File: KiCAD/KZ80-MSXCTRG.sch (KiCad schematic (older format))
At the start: 14 parts, among them J1 MSX SLOT-A, J2 SBC8080 BUS, J3 MEM-SLOT, J4 Z80 CTRL, J5 PPI PORT-A, U1 74HC139, U2 74HC153, U3 74HC32, U4 74HC00

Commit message: 割り込み信号を外部端子と切り替えるジャンパ装備
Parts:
- removed J3: MEM-SLOT, symbol Connector_Generic:Conn_01x02
- added C5, C6: 10u, symbol Device:CP
- added J3: SLT-JP, symbol Connector_Generic:Conn_01x05
- added JP1: INT_JP, symbol Jumper:Jumper_3_Open
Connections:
- net GND: now also C5.1, C6.1; no longer U4.12, U4.13
- net VCC: now also C5.2, C6.2
- net ~CS1: now also U4.1; no longer U4.4
- net ~CS12: now also U4.6; no longer U4.8
- net ~CS2: now also U4.2; no longer U4.5
- net ~INT: now also JP1.1 (A); no longer J1.8 (Pin_8)
- net ~RFSH: now also U4.10, U4.9; no longer U4.1, U4.2
- net ~SLT0: now also J3.1 (Pin_1)
- net ~SLT2: now also J3.2 (Pin_2)
- net ~SLT3: now also U4.12, U4.13, J3.3 (Pin_3)
- net at U3.2: now also U4.8; no longer U4.3
- net at U4.11: now also J3.4 (Pin_4)
- new net: U4.3, U4.4, U4.5
- new net ~INT-J: J3.5 (Pin_5), JP1.3 (B)
- new net ~INT-S: J1.8 (Pin_8), JP1.2 (C)
- no-connect marks 36 -> 34
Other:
- note added: "FRONT SIDE"
- moved on the sheet: C2, C3, C4, U1C, U3B, U3C, U3D, U3E, U4D, U4E

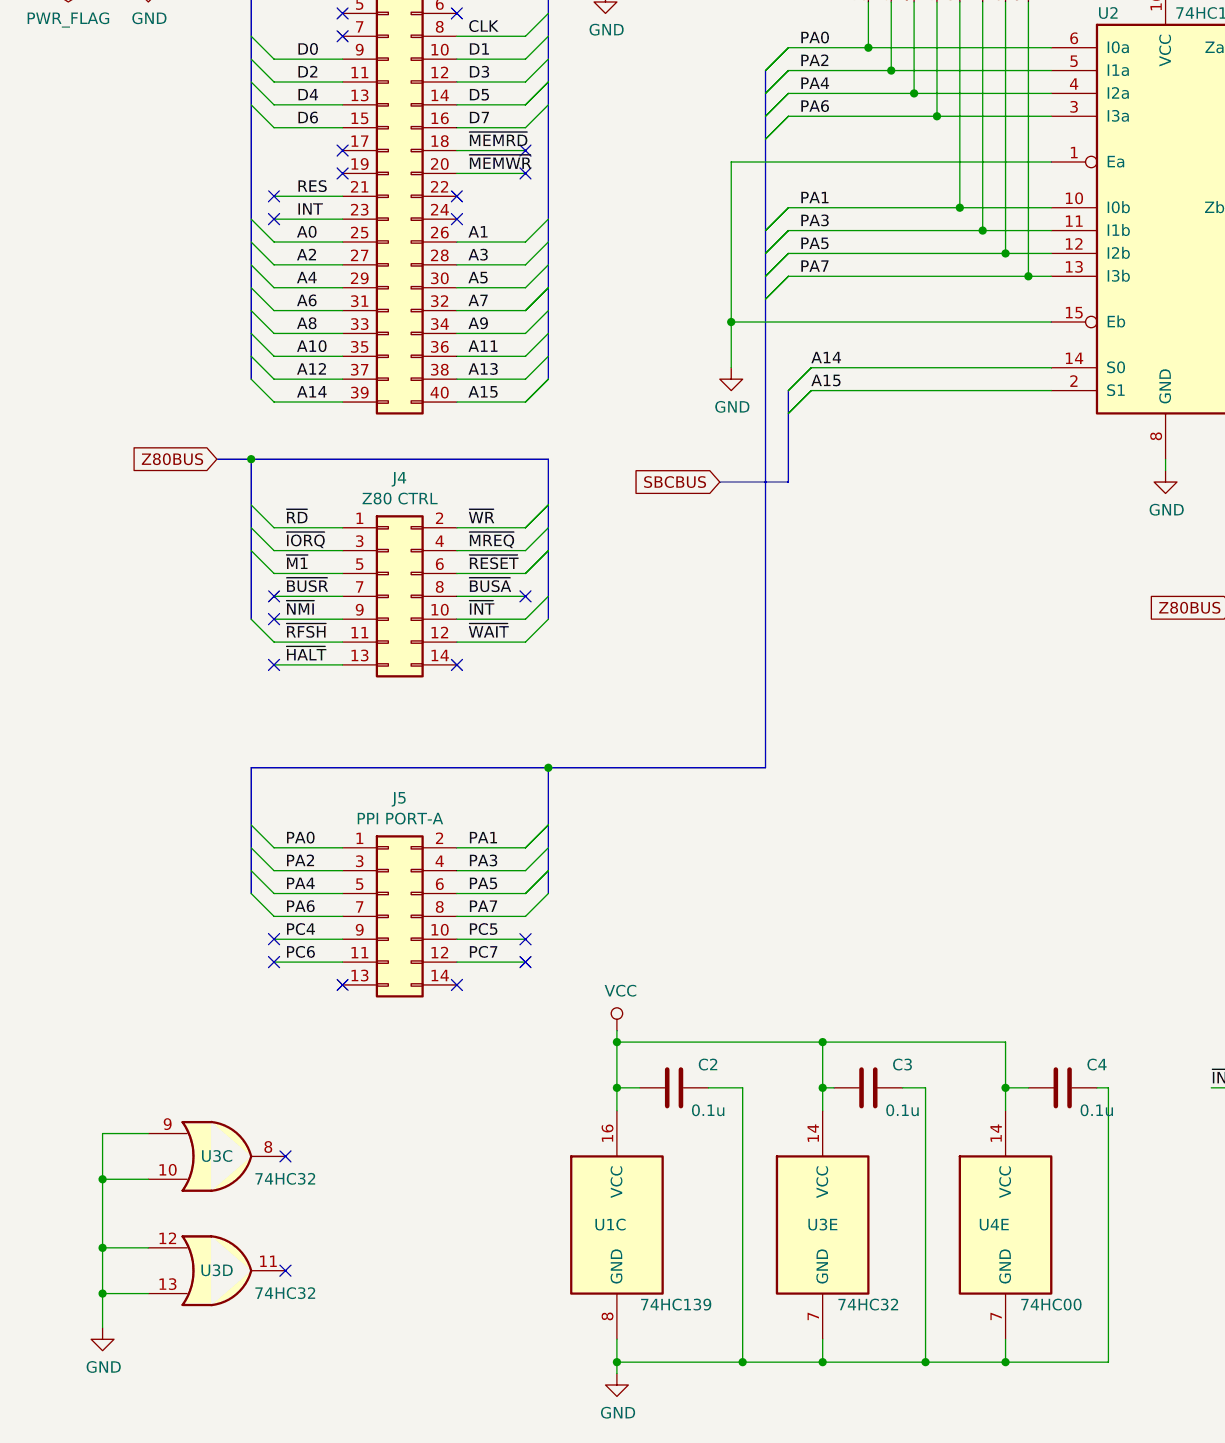
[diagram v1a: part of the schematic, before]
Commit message: 74HC153コントロールをPPI出力で暫定実施
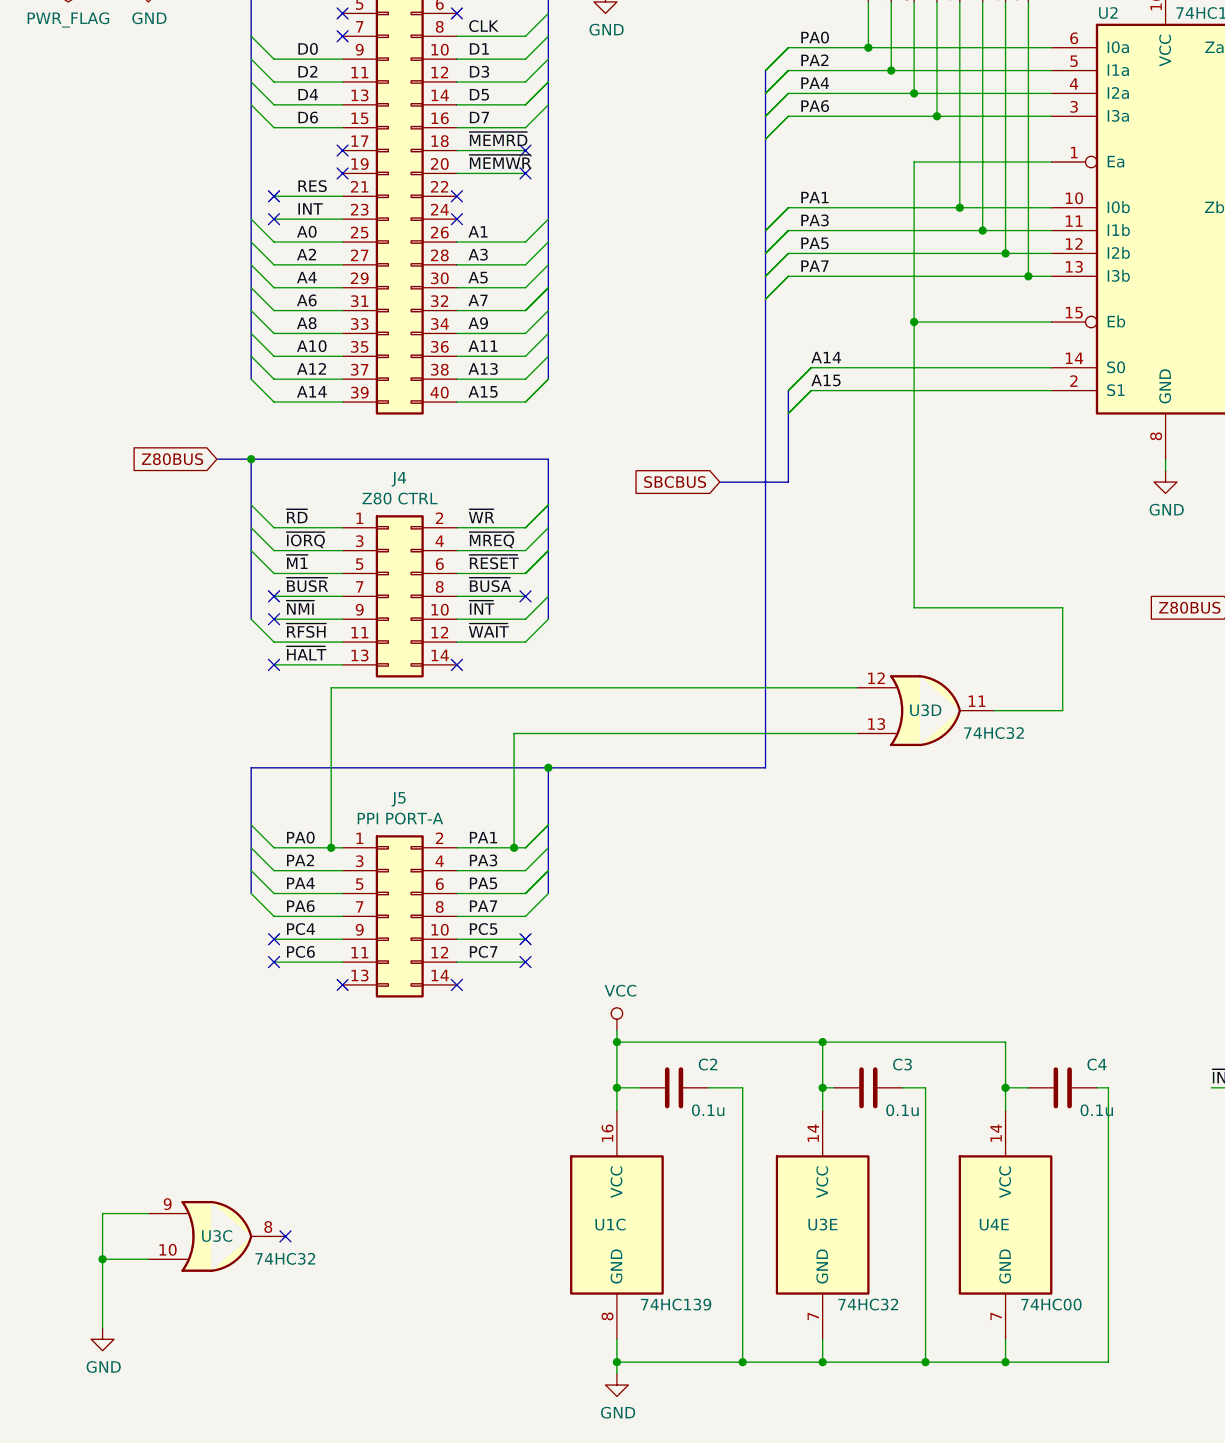
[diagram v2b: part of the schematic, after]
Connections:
- net GND: no longer U2.1 (Ea), U2.15 (Eb), U3.12, U3.13
- net PA0: now also U3.12
- net PA1: now also U3.13
- net at U3.11: now also U2.1 (Ea), U2.15 (Eb)
- no-connect marks 34 -> 33
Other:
- moved on the sheet: U3C, U3D
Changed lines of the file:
@@
 $EndComp
 Wire Wire Line
-	1600 5250 1900 5250
+	1600 5250 1850 5250
 Wire Wire Line
 	1600 5350 1900 5350
@@
 	1500 5450 1600 5550
 Wire Wire Line
-	2400 5250 2700 5250
+	2400 5250 2650 5250
 Wire Wire Line
 	2400 5350 2700 5350
@@
 	2800 4900 3750 4900
 Connection ~ 2800 4900
-$Comp
-L power:GND #PWR08
-U 1 1 5D95374D
-P 3600 3150
-F 0 "#PWR08" H 3600 2900 50  0001 C CNN
-F 1 "GND" H 3605 2977 50  0000 C CNN
-F 2 "" H 3600 3150 50  0001 C CNN
-F 3 "" H 3600 3150 50  0001 C CNN
-	1    3600 3150
-	1    0    0    -1
-$EndComp
-Wire Wire Line
-	5000 2250 3600 2250
-Wire Wire Line
-	3600 2950 5000 2950
-Wire Wire Line
-	3600 2250 3600 2950
-Connection ~ 3600 2950
-Wire Wire Line
-	3600 2950 3600 3150
+Wire Wire Line
+	5000 2250 4400 2250
+Wire Wire Line
+	4400 2950 5000 2950
+Wire Wire Line
+	4400 2250 4400 2950
+Connection ~ 4400 2950
 Text GLabel 3550 3650 0    50   Input ~ 0
 SBCBUS
@@
 L 74xx:74LS32 U3
 U 3 1 5DFAABD4
-P 1350 6600
-F 0 "U3" H 1350 6600 50  0000 C CNN
-F 1 "74HC32" H 1650 6500 50  0000 C CNN
-F 2 "" H 1350 6600 50  0001 C CNN
-F 3 "http://www.ti.com/lit/gpn/sn74LS32" H 1350 6600 50  0001 C CNN
-	3    1350 6600
+P 1350 6950
+F 0 "U3" H 1350 6950 50  0000 C CNN
+F 1 "74HC32" H 1650 6850 50  0000 C CNN
+F 2 "" H 1350 6950 50  0001 C CNN
+F 3 "http://www.ti.com/lit/gpn/sn74LS32" H 1350 6950 50  0001 C CNN
+	3    1350 6950
 	1    0    0    -1
 $EndComp
@@
 L 74xx:74LS32 U3
 U 4 1 5DFAAC92
-P 1350 7100
-F 0 "U3" H 1350 7100 50  0000 C CNN
-F 1 "74HC32" H 1650 7000 50  0000 C CNN
-F 2 "" H 1350 7100 50  0001 C CNN
-F 3 "http://www.ti.com/lit/gpn/sn74LS32" H 1350 7100 50  0001 C CNN
-	4    1350 7100
+P 4450 4650
+F 0 "U3" H 4450 4650 50  0000 C CNN
+F 1 "74HC32" H 4750 4550 50  0000 C CNN
+F 2 "" H 4450 4650 50  0001 C CNN
+F 3 "http://www.ti.com/lit/gpn/sn74LS32" H 4450 4650 50  0001 C CNN
+	4    4450 4650
 	1    0    0    -1
 $EndComp
@@
 $EndComp
 Wire Wire Line
-	850  7200 1050 7200
-Wire Wire Line
-	850  7200 850  7000
-Wire Wire Line
-	850  7000 1050 7000
-Connection ~ 850  7200
-Wire Wire Line
-	850  7000 850  6700
-Wire Wire Line
-	850  6700 1050 6700
-Connection ~ 850  7000
-Wire Wire Line
-	850  6700 850  6500
-Wire Wire Line
-	850  6500 1050 6500
-Connection ~ 850  6700
-NoConn ~ 1650 6600
-NoConn ~ 1650 7100
+	850  7050 1050 7050
+Wire Wire Line
+	850  7050 850  6850
+Wire Wire Line
+	850  6850 1050 6850
+NoConn ~ 1650 6950
 NoConn ~ 8300 4600
 Entry Wire Line
@@
 Wire Wire Line
 	7250 5750 7100 5750
-Wire Wire Line
-	850  7200 850  7350
 $Comp
 L Device:CP C5
@@
 Text Label 7550 5600 0    50   ~ 0
 ~INT-J
+Wire Wire Line
+	850  7350 850  7050
+Connection ~ 850  7050
+Wire Wire Line
+	1850 4550 1850 5250
+Wire Wire Line
+	1850 4550 4150 4550
+Connection ~ 1850 5250
+Wire Wire Line
+	1850 5250 1900 5250
+Wire Wire Line
+	2650 5250 2650 4750
+Wire Wire Line
+	2650 4750 4150 4750
+Connection ~ 2650 5250
+Wire Wire Line
+	2650 5250 2700 5250
+Wire Wire Line
+	4400 4200 5050 4200
+Wire Wire Line
+	5050 4200 5050 4650
+Wire Wire Line
+	5050 4650 4750 4650
+Wire Wire Line
+	4400 2950 4400 4200
 Wire Bus Line
 	6150 4200 6150 4600
